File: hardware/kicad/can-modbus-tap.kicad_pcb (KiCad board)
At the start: 2 copper layers, 124 x 100 mm, 41 parts, among them J1 USB-A plug, J2 USB-C, SW1 BOOT, SW2 RESET, U1 ESP32-S3-WROOM-1-N8, U2 ISO1042BDW, U3 ISO1640BD, U4 ADS1115IDGSR, U5 RFM-0505S, U6 AP7361C-33E-13, U7 AP2112K-3.3

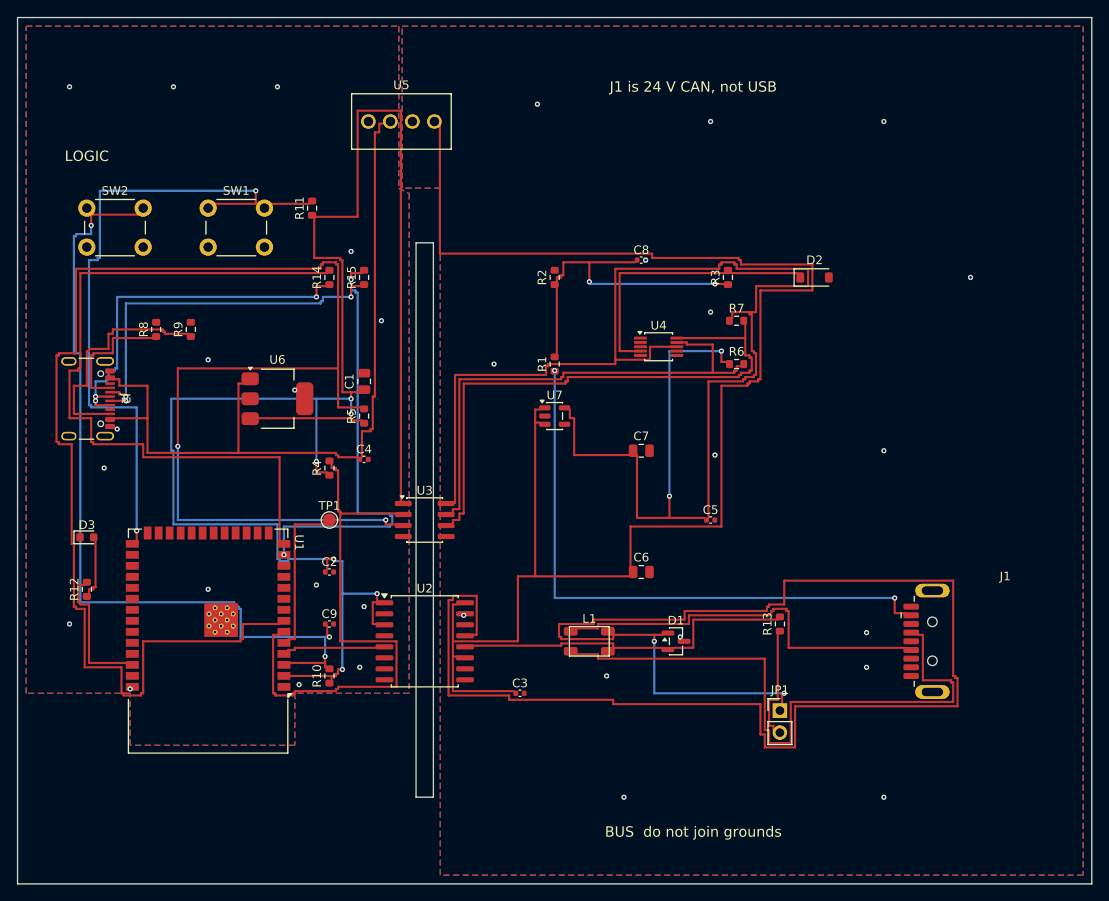
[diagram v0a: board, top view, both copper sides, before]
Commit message: Shrink the routed CAN tap board to 90 by 66 mm.
Co-authored-by: Cursor <cursoragent@cursor.com>
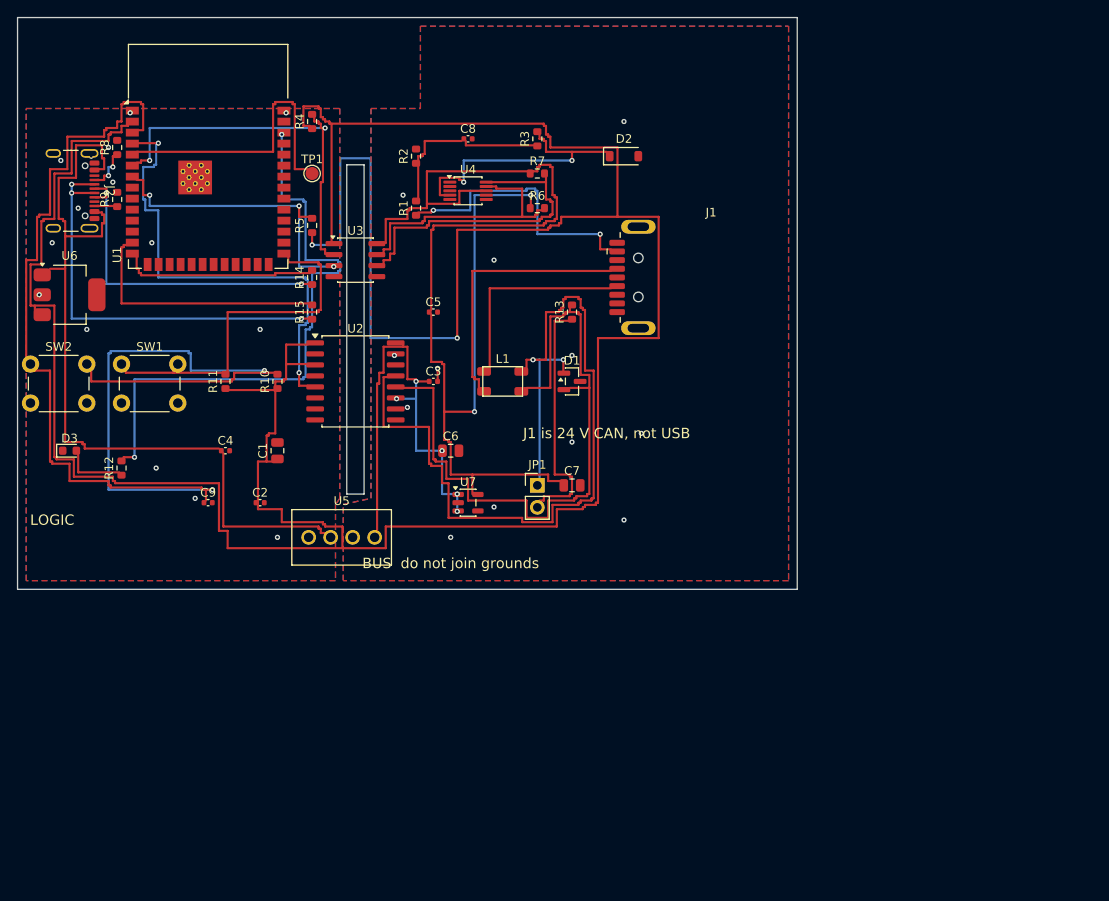
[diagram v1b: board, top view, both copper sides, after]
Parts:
- moved U1 56.0 mm to (22.0, 16.0), turned to 0 degrees
- moved J1 54.0 mm to (80.1, 30.0)
- moved U5 48.5 mm to (33.6, 60.0)
- moved R13 43.3 mm to (64.0, 34.0)
- moved R4 40.0 mm to (34.0, 12.0)
- moved TP1 40.0 mm to (34.0, 18.0)
- moved C5 40.0 mm to (48.0, 34.0)
- moved JP1 38.2 mm to (60.0, 54.0)
- moved C3 37.4 mm to (48.0, 42.0)
- moved R10 34.5 mm to (30.0, 42.0)
- moved D1 32.3 mm to (64.0, 42.0)
- moved L1 31.6 mm to (56.0, 42.0)
- moved U2 31.0 mm to (39.0, 42.0)
- moved U3 31.0 mm to (39.0, 28.0)
- moved R6 29.2 mm to (60.0, 22.0)
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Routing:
- net 3V3_LOG: track 208.2 -> 371.0 mm, vias 6 -> 2
- net SCL_LOG: track 197.8 -> 35.2 mm, vias 2 -> 3
- net 5V_BUS: track 182.2 -> 53.2 mm, vias 0 -> 5
- net CANH: track 192.2 -> 102.2 mm
- net USB_DP: track 85.0 -> 22.5 mm
- net EN: track 95.2 -> 157.0 mm, vias 3 -> 2
- net IO2: track 15.5 -> 69.2 mm, vias 0 -> 2
- net CAN_RX: track 10.8 -> 53.2 mm, vias 0 -> 2
- net CANL: track 38.0 -> 79.0 mm
- net CANL_J: track 70.2 -> 30.2 mm
- net IO0: track 77.8 -> 39.8 mm, vias 2 -> 0
- net 24V: track 68.5 -> 32.0 mm
- net 3V3_BUS: track 177.2 -> 141.0 mm
- net SCL_BUS: track 65.8 -> 37.2 mm
- net SDA_BUS: track 57.2 -> 30.8 mm
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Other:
- board size 124 x 100 mm -> 90 x 66 mm
